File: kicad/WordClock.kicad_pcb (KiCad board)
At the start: 2 copper layers, 384.8 x 111.8 mm, 86 parts, among them J1 USB_B_Micro, J10 GND, J2 Conn_01x01, J3 Conn_01x01, J4 DOut, J5 +5V, J6 +5V, J7 +5V, J8 GND, J9 GND, M1 MicrowaveRadarSensorRCWL-0516, Q1 S8050, Q2 S8050, U1 CP2102-GMR_NRND, U2 AMS1117-3.3, U3 ESP-12E

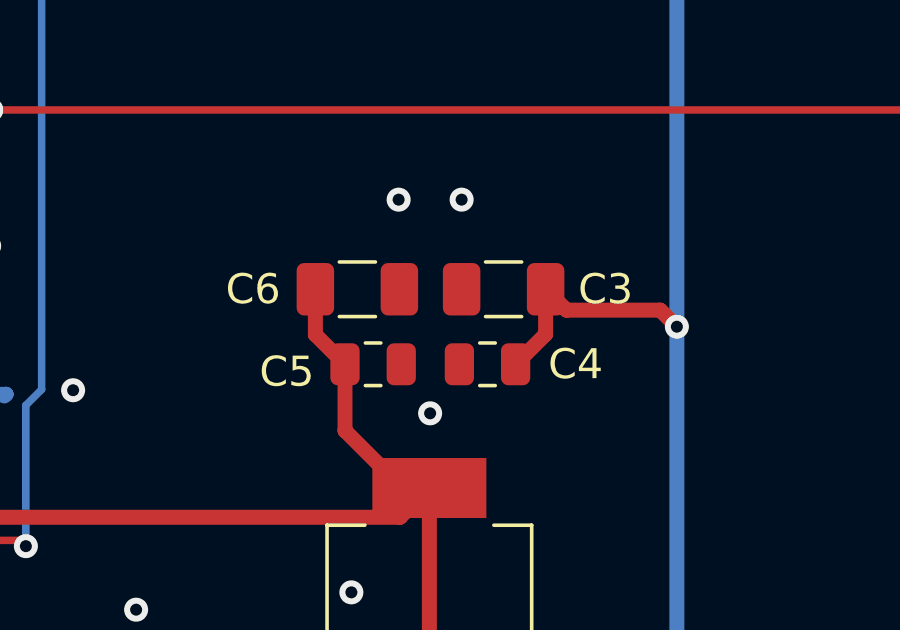
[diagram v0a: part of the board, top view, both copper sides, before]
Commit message: C3+C6 as 0805 instead of 1206
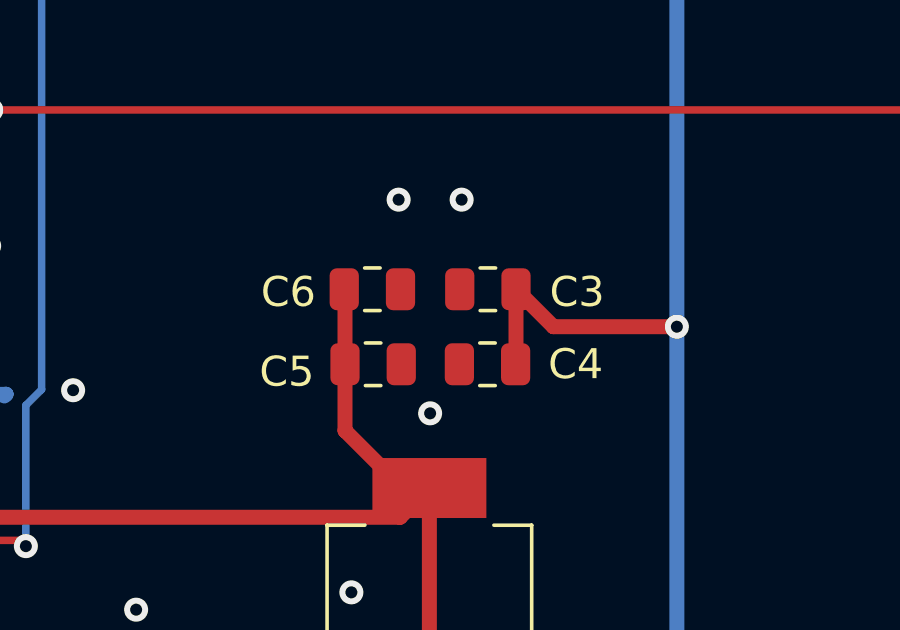
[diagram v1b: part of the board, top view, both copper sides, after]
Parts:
- C3, C6: footprint Capacitor_SMD:C_1206_3216Metric -> Capacitor_SMD:C_0805_2012Metric
- moved C3 0.53 mm to (141.6, 111.5)
- moved C6 0.50 mm to (137.7, 111.5)
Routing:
- net VBUS: track 1701.9 -> 1702.5 mm

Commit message: added LEDs, CP2102 45°
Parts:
- removed J3: Conn_01x01, barn53-kicad:ThroughHolePin1x1
- removed the R9 at (111.5, 110.9)
- added D1: Move, LED_SMD:LED_0805_2012Metric_Castellated, F.Cu at (55.3, 128.2)
- added D2: TxD, LED_SMD:LED_0805_2012Metric_Castellated, F.Cu at (47.7, 128.2)
- added R10: 220, Resistor_SMD:R_0805_2012Metric, F.Cu at (75.7, 116.0)
- added R11: 220, Resistor_SMD:R_0805_2012Metric, F.Cu at (75.7, 114.0)
- J2: value Conn_01x01 -> LDR; footprint barn53-kicad:ThroughHolePin1x1 -> barn53-kicad:ThroughHolePin1x2
- moved R2 11.1 mm to (111.5, 113.0), turned to 180 degrees
- moved C10 3.42 mm to (75.7, 111.7)
- moved R8 2.12 mm to (111.5, 110.9)
- moved U1 1.88 mm to (122.9, 113.2), turned to 315 degrees
- moved J2 1.76 mm to (28.5, 114.2), turned to 270 degrees
- moved R9 0.46 mm to (75.7, 118.1)
- moved R1 0.37 mm to (75.7, 120.1)
- moved R6 0.29 mm to (75.7, 122.1)
- renumbered R10 to R9
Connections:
- LEDM1 pad 4: RxD -> TxD
- R8 pad 1: Move -> +3V3
- R8 pad 2: GND -> Net-(R8-Pad2)
- U1 pad 25: TxD -> RxD
- U1 pad 26: RxD -> TxD
- U3 pad 17: Net-(R9-Pad2) -> Net-(R8-Pad2)
- U3 pad 21: RxD -> TxD
- U3 pad 22: TxD -> RxD
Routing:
- net TxD: track 32.2 -> 202.3 mm, vias 4 -> 9
- net Move: track 231.0 -> 302.2 mm, vias 4 -> 6
- net RxD: track 91.2 -> 35.6 mm, vias 7 -> 4
- net Net-(D2-Pad2): track 0.00 -> 42.7 mm, vias 0 -> 2
- net Net-(D1-Pad2): track 0.00 -> 30.8 mm, vias 0 -> 2
- net Net-(R9-Pad2): track 18.5 -> 0.00 mm, vias 2 -> 0
- net Net-(R8-Pad2): track 0.00 -> 18.5 mm, vias 0 -> 2
- net VDD: track 13.1 -> 27.2 mm
- net GND: track 53.8 -> 65.5 mm, vias 89 -> 91
- net Net-(R2-Pad1): track 20.7 -> 11.9 mm
- net RTS: track 28.8 -> 37.4 mm
- net D+: track 262.7 -> 257.0 mm
- net +3V3: track 127.7 -> 133.4 mm, vias 5 -> 6
- net D-: track 263.1 -> 257.4 mm
- net GPIO0: track 48.0 -> 44.1 mm
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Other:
- board text removed: "LDR"

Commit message: added AND gate to disable WS2812 DIn when flashing
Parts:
- added U4: 74AHC1G08, Package_TO_SOT_SMD:SOT-353_SC-70-5, F.Cu at (131.0, 100.0)
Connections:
- LEDM1 pad 4: TxD -> DIn
- U3 pad 20: Net-(U3-Pad20) -> GPIO5
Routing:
- net GPIO5: track 0.00 -> 59.6 mm, vias 0 -> 4
- net DIn: track 0.00 -> 52.6 mm, vias 0 -> 2
- net TxD: track 202.3 -> 160.9 mm
- net +3V3: track 133.4 -> 156.0 mm, vias 6 -> 8
- net Net-(R8-Pad2): track 18.5 -> 19.1 mm
- net GND: vias 91 -> 96

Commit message: pcb work
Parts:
- moved U4 6.78 mm to (137.6, 101.5)
- moved Q2 5.71 mm to (130.8, 101.5)
- moved Q1 5.40 mm to (125.7, 101.5)
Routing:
- net GPIO5: track 59.6 -> 72.1 mm
- net Net-(Q2-Pad2): track 20.3 -> 30.7 mm
- net Reset: track 91.2 -> 101.5 mm
- net GPIO0: track 44.1 -> 52.2 mm
- net DIn: track 52.6 -> 46.6 mm
- net Net-(Q1-Pad2): track 13.5 -> 18.6 mm
- net TxD: track 160.9 -> 165.0 mm
- net +3V3: track 156.0 -> 155.0 mm
- net DTR: track 26.8 -> 27.7 mm, vias 3 -> 4
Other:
- board text added: "WordClock rev.A 11/19"
- board text added: "barn53.de"

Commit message: minor
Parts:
- moved J1 0.24 mm to (350.1, 91.5)
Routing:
- net GND: track 65.5 -> 66.6 mm, vias 96 -> 95
- net VBUS: track 1705.4 -> 1706.4 mm

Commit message: painful error!
Q1 and Q2 had the wrong pins with footprint SO-23!!!!! Added new S8050_J3 Symbol in barn32-kicad library with correct pinning.
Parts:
- Q1, Q2: value S8050 -> S8050_J3Y
- moved Q2 0.13 mm to (130.9, 101.5)
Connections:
- Q1 pad 1: RTS -> Net-(Q1-Pad1)
- Q1 pad 2: Net-(Q1-Pad2) -> RTS
- Q2 pad 1: DTR -> Net-(Q2-Pad1)
- Q2 pad 2: Net-(Q2-Pad2) -> DTR
- R3 pad 1: Net-(Q1-Pad2) -> Net-(Q1-Pad1)
- R4 pad 1: Net-(Q2-Pad2) -> Net-(Q2-Pad1)
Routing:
- net Net-(Q2-Pad2): track 30.7 -> 0.00 mm, vias 2 -> 0
- net Net-(Q2-Pad1): track 0.00 -> 25.7 mm, vias 0 -> 2
- net Net-(Q1-Pad1): track 0.00 -> 21.2 mm, vias 0 -> 2
- net Net-(Q1-Pad2): track 18.6 -> 0.00 mm, vias 2 -> 0
- net GPIO0: track 52.2 -> 51.0 mm
- net RTS: track 37.0 -> 36.1 mm
- net DTR: track 27.7 -> 28.4 mm
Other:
- board text added: "WordClock rev.B 11/19"
- board text removed: "WordClock rev.A 11/19"

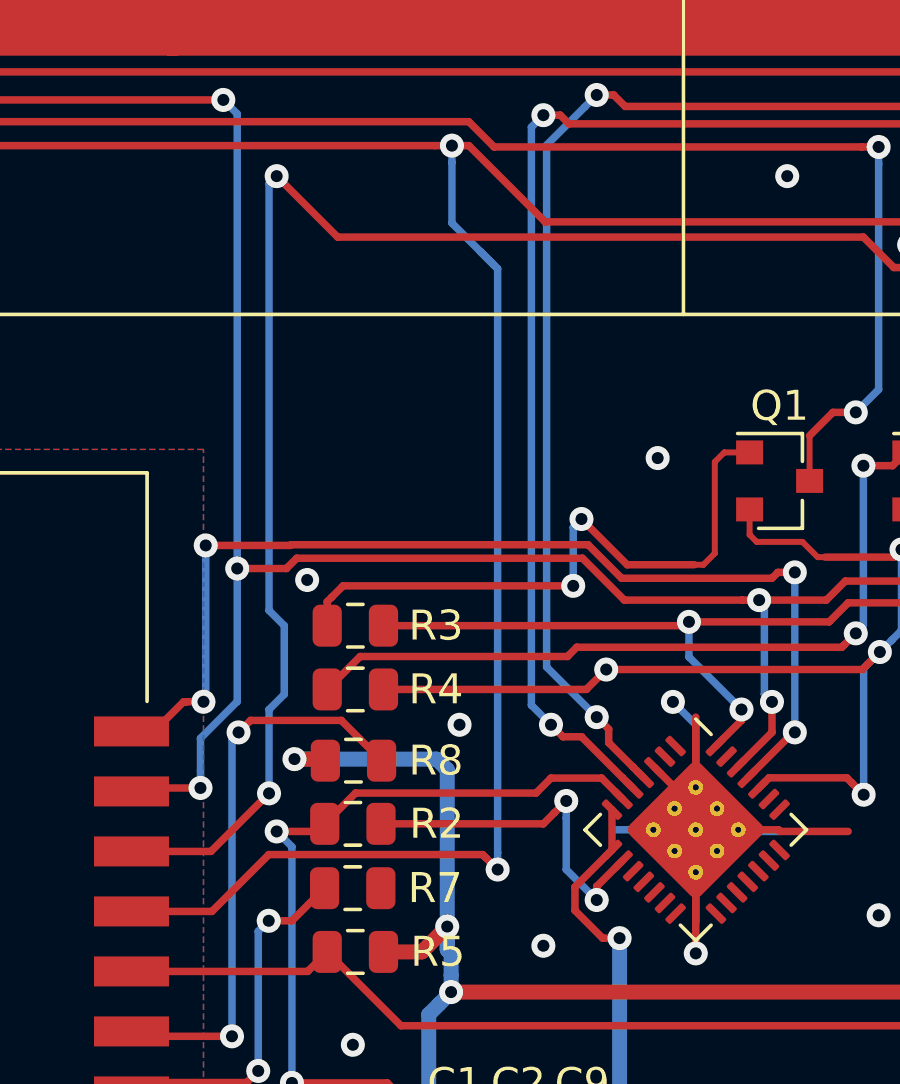
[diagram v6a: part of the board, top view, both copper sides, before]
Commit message: Added missing pull down resistor
Aaaaaargh!
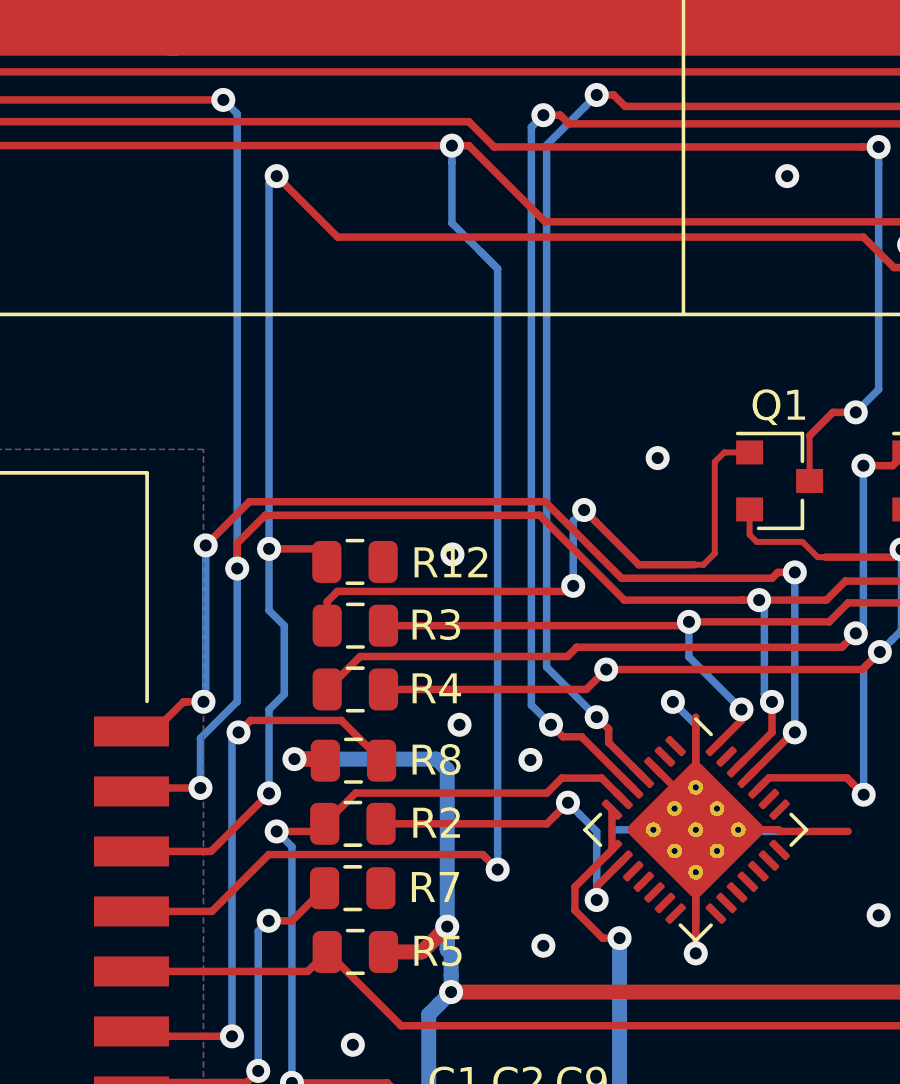
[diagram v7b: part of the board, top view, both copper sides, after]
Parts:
- added R12: 10k, Resistor_SMD:R_0805_2012Metric, F.Cu at (111.5, 104.2)
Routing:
- net GPIO5: track 72.1 -> 74.2 mm, vias 4 -> 5
- net TxD: track 164.7 -> 166.4 mm
- net RxD: track 35.8 -> 37.0 mm
- net GND: vias 95 -> 96

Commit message: Update WordClock.kicad_pcb
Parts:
- turned D2 to 0 degrees
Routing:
- net Net-(D2-Pad2): track 42.7 -> 37.1 mm
- net TxD: track 166.4 -> 169.3 mm
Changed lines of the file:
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@@
-(kicad_pcb (version 20171130) (host pcbnew "(5.1.4)-1")
+(kicad_pcb (version 20171130) (host pcbnew "(5.1.4-0-10_14)")
   (general
     (thickness 1.6)
     (drawings 25)
-    (tracks 984)
+    (tracks 988)
     (zones 0)
     (modules 90)
@@
   )
   (module LED_SMD:LED_0805_2012Metric_Castellated (layer F.Cu)
-    (at 47.726 128.22 180)
+    (at 47.726 128.22)
     (descr "LED SMD 0805 (2012 Metric), castellated end terminal, IPC_7351 nominal, (Body size source: https://docs.google.com/spreadsheets/d/1BsfQQcO9C6DZCsRaXUlFlo91Tg2WpOkGARC1WS5S8t0/edit?usp=sharing), generated with kicad-footprint-generator")
     (tags "LED castellated")
     (attr smd)
-    (fp_text reference D2 (at 3.048 -0.254) (layer F.SilkS) hide
+    (fp_text reference D2 (at -3.048 0.254) (layer F.SilkS) hide
       (effects (font (size 1 1) (thickness 0.15)))
     )
-    (fp_text value TxD (at 0 1.778) (layer F.SilkS)
+    (fp_text value TxD (at -0.762 -1.778) (layer F.SilkS)
       (effects (font (size 1 1) (thickness 0.15)))
     )
@@
     (fp_line (start -0.7 -0.6) (end -1 -0.3) (layer F.Fab) (width 0.1))
     (fp_line (start 1 -0.6) (end -0.7 -0.6) (layer F.Fab) (width 0.1))
-    (pad 2 smd roundrect (at 0.9625 0 180) (size 1.325 1.3) (layers F.Cu F.Paste F.Mask) (roundrect_rratio 0.192308)
+    (pad 2 smd roundrect (at 0.9625 0) (size 1.325 1.3) (layers F.Cu F.Paste F.Mask) (roundrect_rratio 0.192308)
       (net 75 "Net-(D2-Pad2)"))
-    (pad 1 smd roundrect (at -0.9625 0 180) (size 1.325 1.3) (layers F.Cu F.Paste F.Mask) (roundrect_rratio 0.192308)
+    (pad 1 smd roundrect (at -0.9625 0) (size 1.325 1.3) (layers F.Cu F.Paste F.Mask) (roundrect_rratio 0.192308)
       (net 47 TxD))
     (model ${KISYS3DMOD}/LED_SMD.3dshapes/LED_0805_2012Metric_Castellated.wrl
@@
   (segment (start 107.625 89.313) (end 107.162 88.85) (width 0.25) (layer B.Cu) (net 47))
   (segment (start 107.625 104.47) (end 107.625 89.313) (width 0.25) (layer B.Cu) (net 47))
-  (via (at 48.742 88.85) (size 0.8) (drill 0.4) (layers F.Cu B.Cu) (net 47))
-  (segment (start 107.162 88.85) (end 48.742 88.85) (width 0.25) (layer F.Cu) (net 47))
-  (segment (start 48.742 88.85) (end 48.742 126.188) (width 0.25) (layer B.Cu) (net 47))
-  (via (at 50.266 127.712) (size 0.8) (drill 0.4) (layers F.Cu B.Cu) (net 47))
-  (segment (start 48.742 126.188) (end 50.266 127.712) (width 0.25) (layer B.Cu) (net 47))
-  (segment (start 49.1965 127.712) (end 48.6885 128.22) (width 0.25) (layer F.Cu) (net 47))
-  (segment (start 50.266 127.712) (end 49.1965 127.712) (width 0.25) (layer F.Cu) (net 47))
   (segment (start 107.625 104.47) (end 107.625 108.903998) (width 0.25) (layer B.Cu) (net 47))
   (segment (start 107.625 108.903998) (end 106.4 110.128998) (width 0.25) (layer B.Cu) (net 47))
@@
   (segment (start 107.625 104.47) (end 107.625 103.627) (width 0.25) (layer F.Cu) (net 47))
   (segment (start 107.625 103.627) (end 108.559 102.693) (width 0.25) (layer F.Cu) (net 47))
+  (via (at 44.678 126.696) (size 0.8) (drill 0.4) (layers F.Cu B.Cu) (net 47))
+  (segment (start 44.678 126.696) (end 44.678 89.612001) (width 0.25) (layer B.Cu) (net 47))
+  (segment (start 45.331999 88.958002) (end 44.932 89.358001) (width 0.25) (layer F.Cu) (net 47))
+  (segment (start 45.440001 88.85) (end 45.331999 88.958002) (width 0.25) (layer F.Cu) (net 47))
+  (segment (start 44.678 89.612001) (end 44.932 89.358001) (width 0.25) (layer B.Cu) (net 47))
+  (via (at 44.932 89.358001) (size 0.8) (drill 0.4) (layers F.Cu B.Cu) (net 47))
+  (segment (start 107.162 88.85) (end 45.440001 88.85) (width 0.25) (layer F.Cu) (net 47))
+  (segment (start 46.202 128.22) (end 46.7635 128.22) (width 0.25) (layer F.Cu) (net 47))
+  (segment (start 44.678 126.696) (end 46.202 128.22) (width 0.25) (layer F.Cu) (net 47))
   (segment (start 31.55 39.85) (end 31.49 39.79) (width 0.25) (layer F.Cu) (net 48))
   (segment (start 32.55 39.85) (end 31.55 39.85) (width 0.25) (layer F.Cu) (net 48) (status 10))
@@
   (segment (start 73.74949 117.00701) (end 58.197685 117.00701) (width 0.25) (layer F.Cu) (net 74))
   (segment (start 57.886 117.26101) (end 57.632 117.00701) (width 0.25) (layer B.Cu) (net 74))
-  (via (at 45.186 127.458) (size 0.8) (drill 0.4) (layers F.Cu B.Cu) (net 75))
-  (segment (start 46.0015 127.458) (end 46.7635 128.22) (width 0.25) (layer F.Cu) (net 75))
-  (segment (start 45.186 127.458) (end 46.0015 127.458) (width 0.25) (layer F.Cu) (net 75))
-  (via (at 45.694002 117.298) (size 0.8) (drill 0.4) (layers F.Cu B.Cu) (net 75))
-  (segment (start 45.186 117.806002) (end 45.294003 117.697999) (width 0.25) (layer B.Cu) (net 75))
-  (segment (start 45.186 127.458) (end 45.186 117.806002) (width 0.25) (layer B.Cu) (net 75))
-  (segment (start 45.294003 117.697999) (end 45.694002 117.298) (width 0.25) (layer B.Cu) (net 75))
-  (segment (start 46.710002 116.282) (end 46.094001 116.898001) (width 0.25) (layer F.Cu) (net 75))
-  (segment (start 46.094001 116.898001) (end 45.694002 117.298) (width 0.25) (layer F.Cu) (net 75))
-  (segment (start 72.4425 116.282) (end 46.710002 116.282) (width 0.25) (layer F.Cu) (net 75))
+  (via (at 51.028002 117.044) (size 0.8) (drill 0.4) (layers F.Cu B.Cu) (net 75))
   (segment (start 74.7285 113.996) (end 72.4425 116.282) (width 0.25) (layer F.Cu) (net 75))
+  (segment (start 51.428001 116.644001) (end 51.028002 117.044) (width 0.25) (layer F.Cu) (net 75))
+  (segment (start 72.4425 116.282) (end 51.790002 116.282) (width 0.25) (layer F.Cu) (net 75))
+  (segment (start 51.790002 116.282) (end 51.428001 116.644001) (width 0.25) (layer F.Cu) (net 75))
+  (via (at 50.266 126.696002) (size 0.8) (drill 0.4) (layers F.Cu B.Cu) (net 75))
+  (segment (start 51.028002 117.044) (end 50.266 117.806002) (width 0.25) (layer B.Cu) (net 75))
+  (segment (start 50.266 117.806002) (end 50.266 126.130317) (width 0.25) (layer B.Cu) (net 75))
+  (segment (start 50.266 126.130317) (end 50.266 126.696002) (width 0.25) (layer B.Cu) (net 75))
+  (segment (start 50.212498 126.696002) (end 48.6885 128.22) (width 0.25) (layer F.Cu) (net 75))
+  (segment (start 50.266 126.696002) (end 50.212498 126.696002) (width 0.25) (layer F.Cu) (net 75))
   (via (at 107.45 120.0625) (size 0.8) (drill 0.4) (layers F.Cu B.Cu) (net 76))
   (segment (start 104.2625 120.0625) (end 104.1 119.9) (width 0.25) (layer F.Cu) (net 76) (status 30))
@@
   (segment (start 122.86 104.344) (end 121.012908 104.344) (width 0.25) (layer F.Cu) (net 79))
   (segment (start 118.6395 105.233) (end 118.825 105.0475) (width 0.25) (layer F.Cu) (net 79))
-  (segment (start 110.967 105.233) (end 118.6395 105.233) (width 0.25) (layer F.Cu) (net 79))
-  (segment (start 110.625 106.375) (end 110.625 105.575) (width 0.25) (layer F.Cu) (net 79))
-  (segment (start 110.625 105.575) (end 110.967 105.233) (width 0.25) (layer F.Cu) (net 79))
+  (segment (start 118.259315 105.0475) (end 118.825 105.0475) (width 0.25) (layer F.Cu) (net 79))
+  (segment (start 118.031805 105.27501) (end 118.259315 105.0475) (width 0.25) (layer F.Cu) (net 79))
+  (segment (start 110.80299 105.27501) (end 118.031805 105.27501) (width 0.25) (layer F.Cu) (net 79))
+  (segment (start 110.625 105.453) (end 110.80299 105.27501) (width 0.25) (layer F.Cu) (net 79))
+  (segment (start 110.625 106.375) (end 110.625 105.453) (width 0.25) (layer F.Cu) (net 79))
   (via (at 128.498 101.042) (size 0.8) (drill 0.4) (layers F.Cu B.Cu) (net 80))
   (segment (start 129.469 101.042) (end 129.911 100.6) (width 0.25) (layer F.Cu) (net 80))
